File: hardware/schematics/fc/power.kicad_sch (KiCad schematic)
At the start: 36 parts, among them Q10 DMN1150UFB-7B, U10 NCV8187AMT180TAG, U11 LP5912-3.3DRVR, U7 LMR51420YFDDCR, U8 LMR51420YFDDCR, U9 TPS2116DRLR

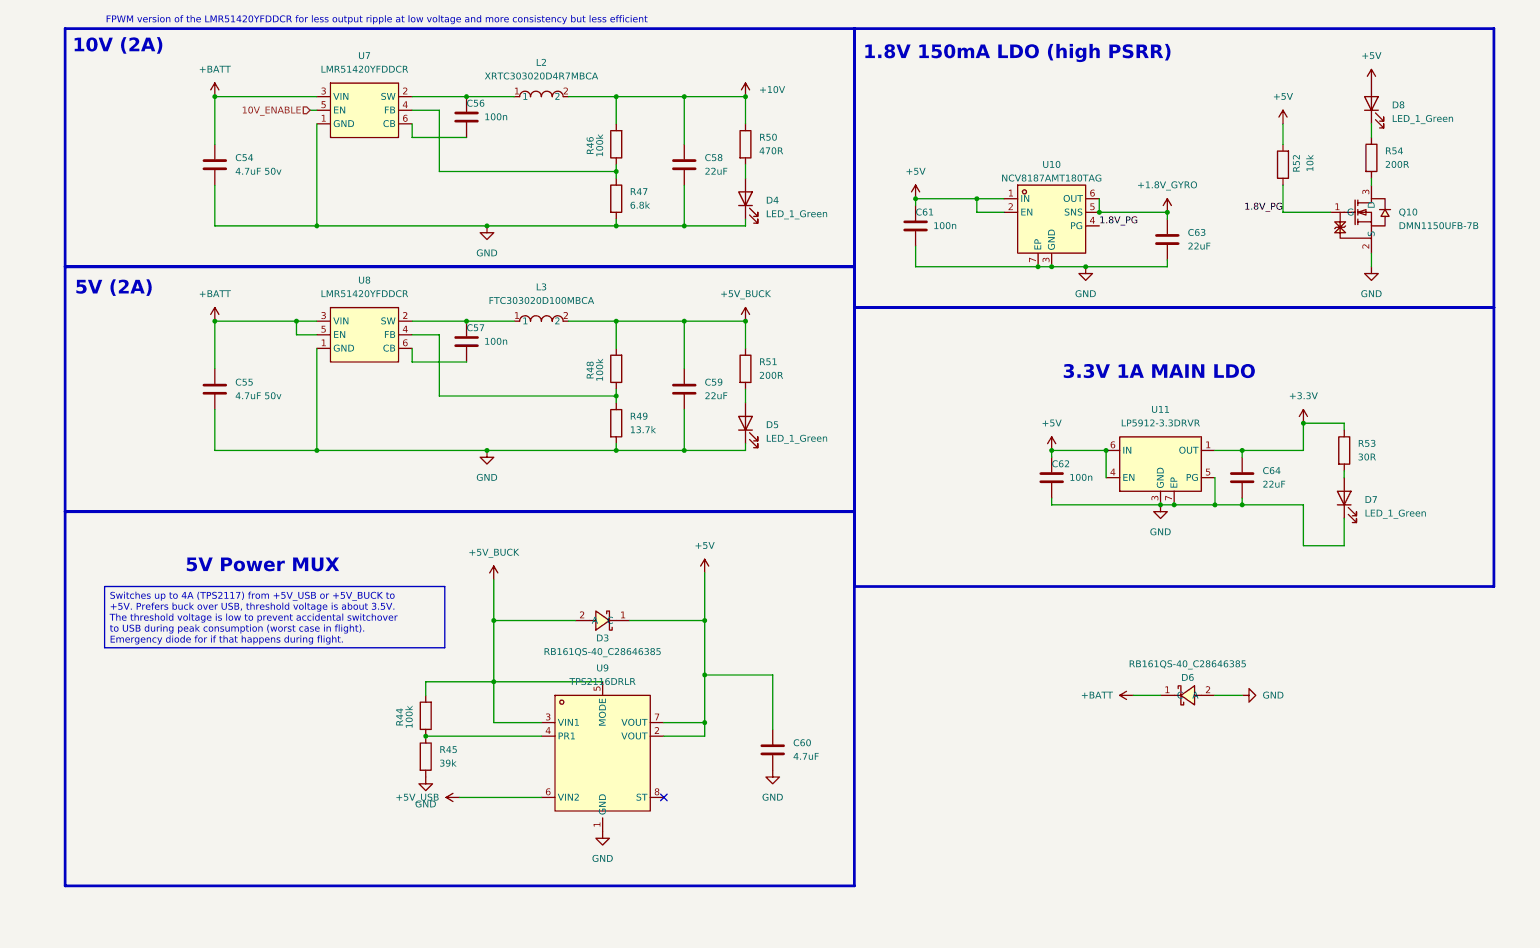
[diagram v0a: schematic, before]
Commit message: Refresh design sources: import rev2 sheets + libs from current sibling repos
FC sheets   <- OpenFC-Lite-Mini rev2 (RP2354A, LMR51430 power tree, COS8051 OSD)
ESC sheets  <- 4in1-mini Rev2 (AT32F421 + NSG2065Q + DOY180N03T, INA186 CSA)
ELRS sheet  <- OpenRX-Lite (ESP32-C3 + SX1281, chip antenna)

Drop-in swaps at paths the root sheet already references; esc_channel
instantiated 4x from root resolves. esc_main.kicad_sch (4in1-mini top:
buck/LDO/CSA/TVS/connector) kept as reference, with ESC.kicad_sch beside
it so its internal channel instances resolve if ever instantiated.

Libraries replaced wholesale: lib(.kicad_sym/.pretty/.3dshapes) from
OpenFC-Lite-Mini, components+4in1ESC from 4in1-mini, OpenRX-Shared from
OpenRX. 3D model paths in OpenRX-Shared.pretty rewritten to project-
local via pcbnew API. Hierarchy verified with kicad-cli netlist export.

Supersedes the 2026-04 port from OpenFC-ECO V0.3 / 4in1ESC 2 (in git
history). Schematic re-annotation + root rewiring is manual work in
KiCad. Old PCB layout retained; footprints are embedded so it opens,
but layout predates this refresh.

Co-Authored-By: Claude Fable 5 <noreply@anthropic.com>
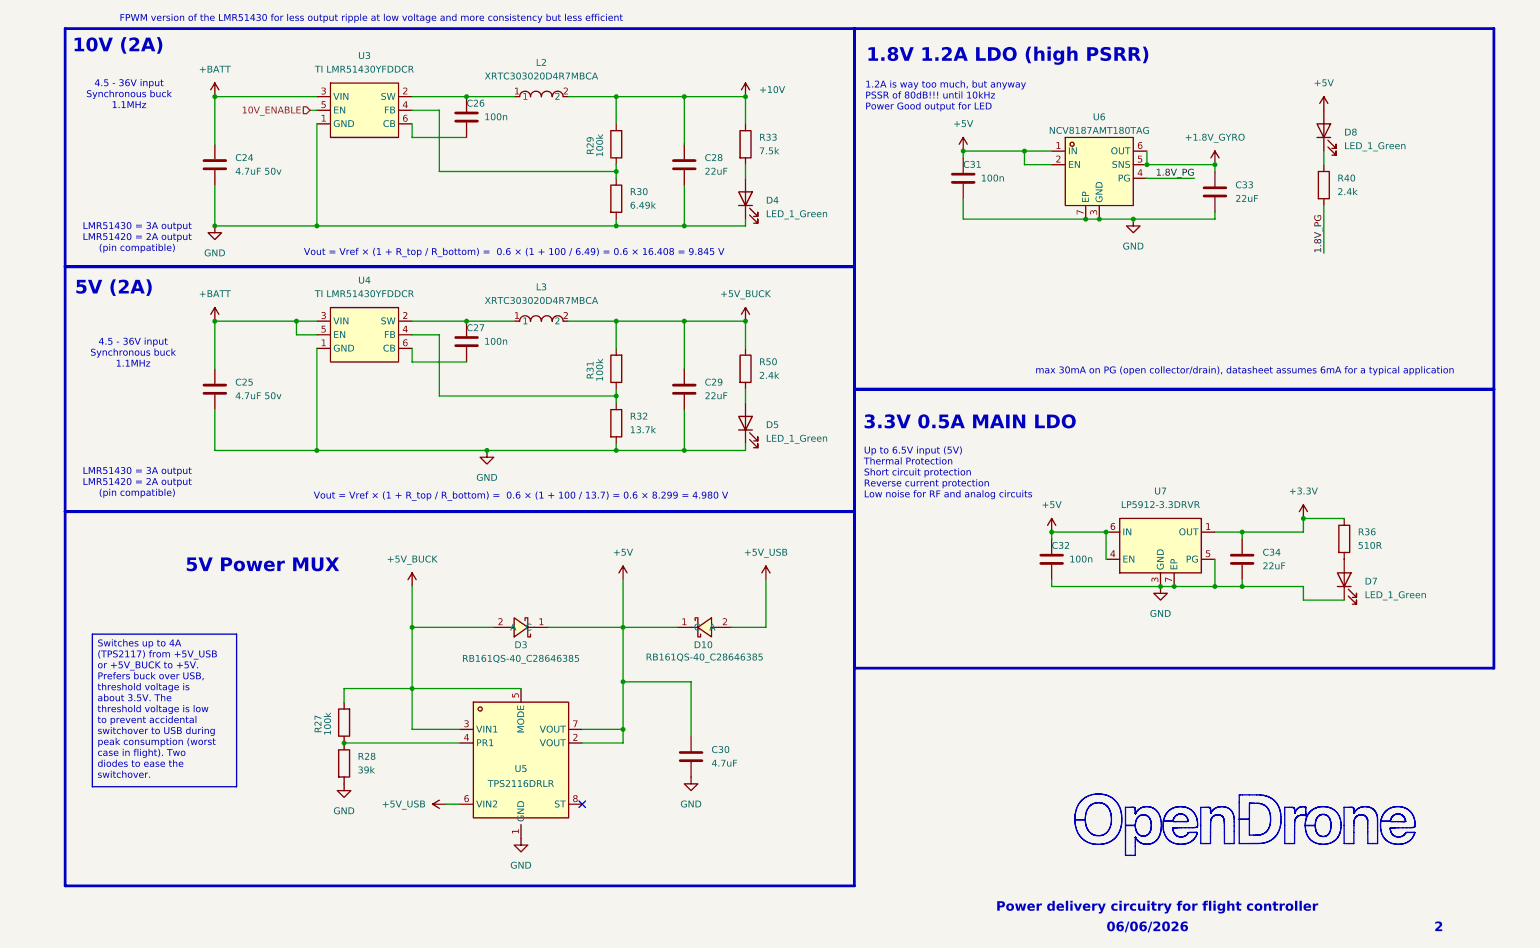
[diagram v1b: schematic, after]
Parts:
- removed D6: RB161QS-40_C28646385, lib:SOD-882_L1.0-W0.6-RD, symbol lib:RB161QS-40_C28646385
- removed Q10: DMN1150UFB-7B, lib:DFN-3L_L1.0-W0.6-P0.65-BR, symbol lib:DMN1150UFB-7B
- removed R51: 200R, Resistor_SMD:R_0201_0603Metric, symbol Device:R
- removed R52: 10k, Resistor_SMD:R_0201_0603Metric, symbol Device:R
- added D10: RB161QS-40_C28646385, lib:SOD-882_L1.0-W0.6-RD, symbol lib:RB161QS-40_C28646385
- added R50: 2.4k, Resistor_SMD:R_0201_0603Metric, symbol Device:R
- D3: LCSC (none) -> C28646385; LCSC Part C28646385 -> (none)
- D4, D5, D7, D8: footprint LED_SMD:LED_0201_0603Metric -> LED_SMD:LED_0402_1005Metric; LCSC C3646922 -> C965793; MPN XL-0201UGC -> XL-1005UGC
- L2: LCSC (none) -> C39846837; LCSC Part C39846837 -> (none)
- L3: value FTC303020D100MBCA -> XRTC303020D4R7MBCA; LCSC (none) -> C39846837; LCSC Part C7423323 -> (none)
- R30: renamed from R47; value 6.8k -> 6.49k; LCSC C274877 -> C2107920; MPN RC0201FR-076K8L -> (none); Manufacturer YAGEO -> (none)
- R33: renamed from R50; value 470R -> 7.5k; LCSC C473464 -> C474437; MPN 0201WMF4700TEE -> (none); Manufacturer UNI-ROYAL -> (none)
- R36: renamed from R53; value 30R -> 510R; LCSC C778391 -> C57784; MPN NQ01WMJ0300TEE -> (none); Manufacturer UNI-ROYAL -> (none)
- R40: renamed from R54; value 200R -> 2.4k; LCSC C270359 -> C166281; MPN 0201WMF2000TEE -> (none); Manufacturer UNI-ROYAL -> (none)
- U3: renamed from U7; value LMR51420YFDDCR -> TI LMR51430YFDDCR; footprint lib:SOT-23-6_L2.9-W1.6-P0.95-LS2.9-BL__lib -> lib:SOT-23-6_L2.9-W1.6-P0.95-LS2.9-BL; LCSC (none) -> C5219261; LCSC Part C7296200 -> (none); MPN LMR51420YFDDCR -> TI LMR51430YFDDCR
- U4: renamed from U8; value LMR51420YFDDCR -> TI LMR51430YFDDCR; footprint lib:SOT-23-6_L2.9-W1.6-P0.95-LS2.9-BL__lib -> lib:SOT-23-6_L2.9-W1.6-P0.95-LS2.9-BL; LCSC (none) -> C5219261; LCSC Part C7296200 -> (none); MPN LMR51420YFDDCR -> TI LMR51430YFDDCR
- U5: renamed from U9; LCSC (none) -> C3235557; LCSC Part C3235557 -> (none)
- U6: renamed from U10; LCSC (none) -> C893189; LCSC Part C893189 -> (none)
- renumbered C54 to C24, C55 to C25, C56 to C26, C57 to C27, C58 to C28, C59 to C29, C60 to C30, C61 to C31, C62 to C32, C63 to C33, C64 to C34, R44 to R27, R45 to R28, R46 to R29, R48 to R31, R49 to R32, U11 to U7
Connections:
- net +5V: now also D10.1 (C)
- net +5V_BUCK: now also R50.1
- net +5V_USB: now also D10.2 (A)
- net 1.8V_PG: now also R40.2
- net at D5.2 (A): now also R50.2
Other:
- note added: "06/06/2026"
- note added: "1.2A is way too much, but anyway PSSR of 80dB!!! until 10kHz Power Good output for LED"
- note added: "1.8V 1.2A LDO (high PSRR)"
- note added: "2"
- note added: "3.3V 0.5A MAIN LDO"
- note added: "4.5 - 36V input Synchronous buck 1.1MHz"
- note added: "FPWM version of the LMR51430 for less output ripple at low voltage and more consistency but less efficient"
- note added: "LMR51430 = 3A output LMR51420 = 2A output (pin compatible)"
- note added: "Power delivery circuitry for flight controller"
- note added: "Up to 6.5V input (5V) Thermal Protection Short circuit protection Reverse current protection Low noise for RF and analog circuits"
- note added: "Vout = Vref × (1 + R_top / R_bottom) = 0.6 × (1 + 100 / 13.7) = 0.6 × 8.299 = 4.980 V"
- note added: "Vout = Vref × (1 + R_top / R_bottom) = 0.6 × (1 + 100 / 6.49) = 0.6 × 16.408 = 9.845 V"
- note added: "max 30mA on PG (open collector/drain), datasheet assumes 6mA for a typical application"
- note removed: "1.8V 150mA LDO (high PSRR)"
- note removed: "3.3V 1A MAIN LDO"
- note removed: "FPWM version of the LMR51420YFDDCR for less output ripple at low voltage and more consistency but less efficient"
- moved on the sheet: C30, C31, C32, C33, C34, D3, R27, R28, R36, R40, U5, U6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
